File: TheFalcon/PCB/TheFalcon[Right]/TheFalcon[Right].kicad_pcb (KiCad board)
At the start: 4 copper layers, 173.3 x 142.5 mm, 166 parts, among them IC1 IS31FL3729-QFLS4-TR, J1 Conn_01x01, J2 Conn_01x01, J3 Conn_01x01, J4 Conn_01x01, J5 Conn_01x04_Pin, J6 Conn_01x01, J7 Conn_01x01, J8 Conn_01x01, SW1 SW_Push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

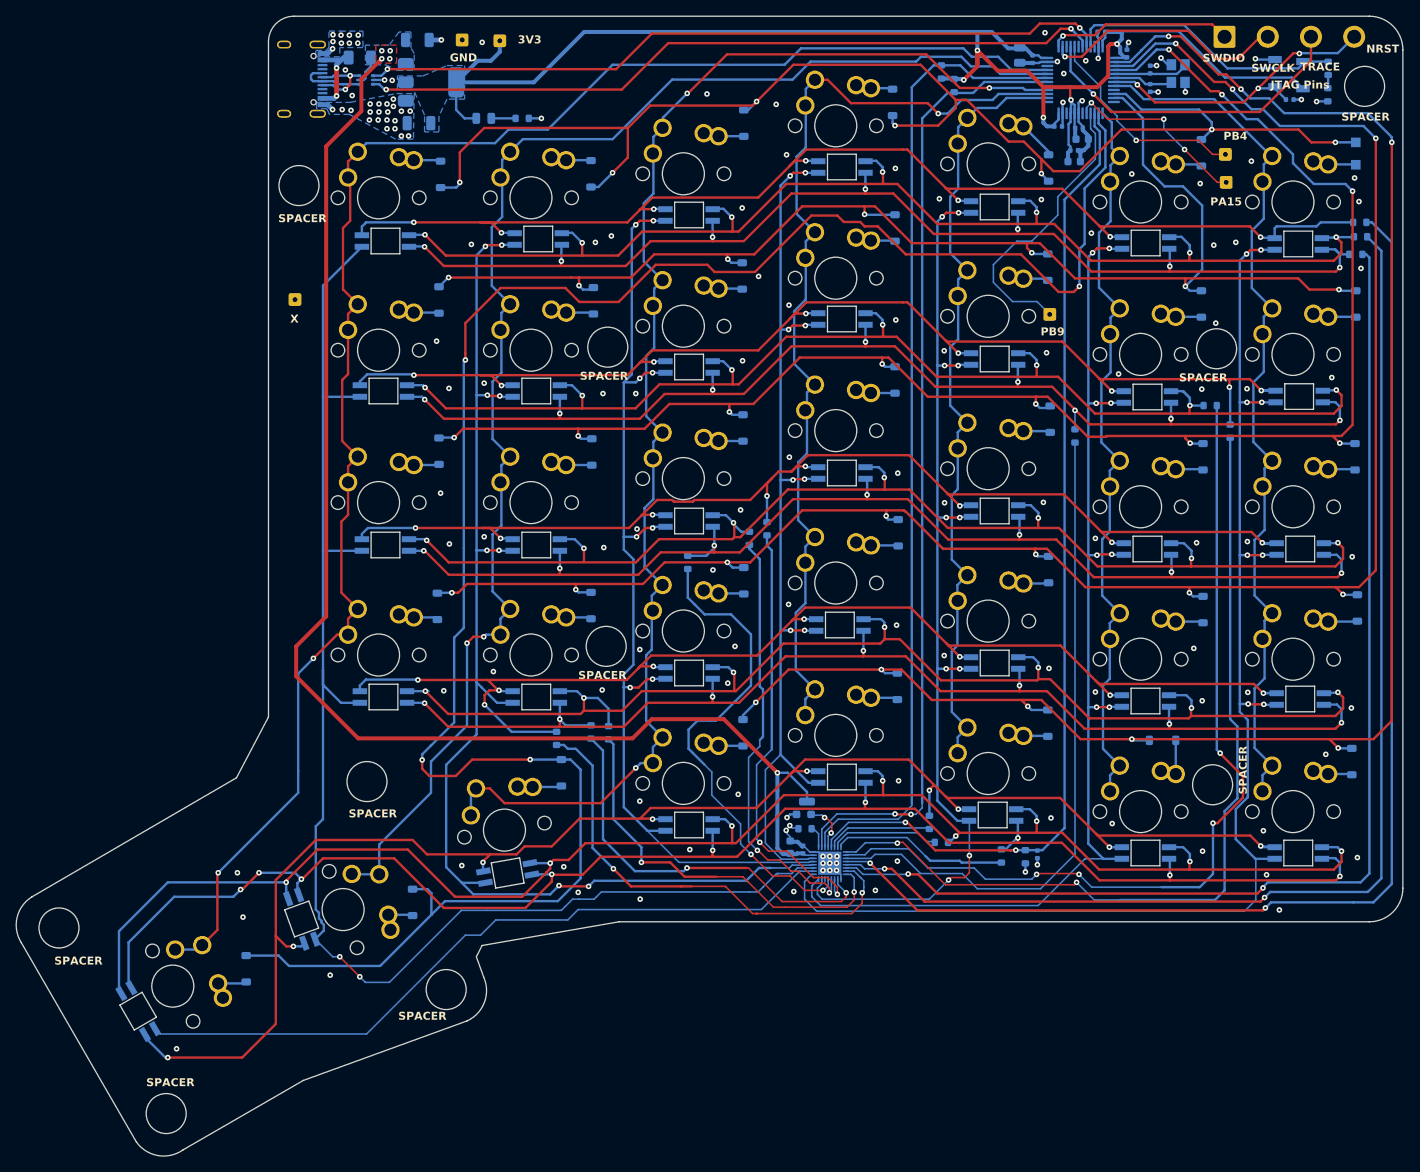
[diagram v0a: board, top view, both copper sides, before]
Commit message: Save
Checked right PCB and hole to track spacing for left. Will do check for left pcb tomorrow
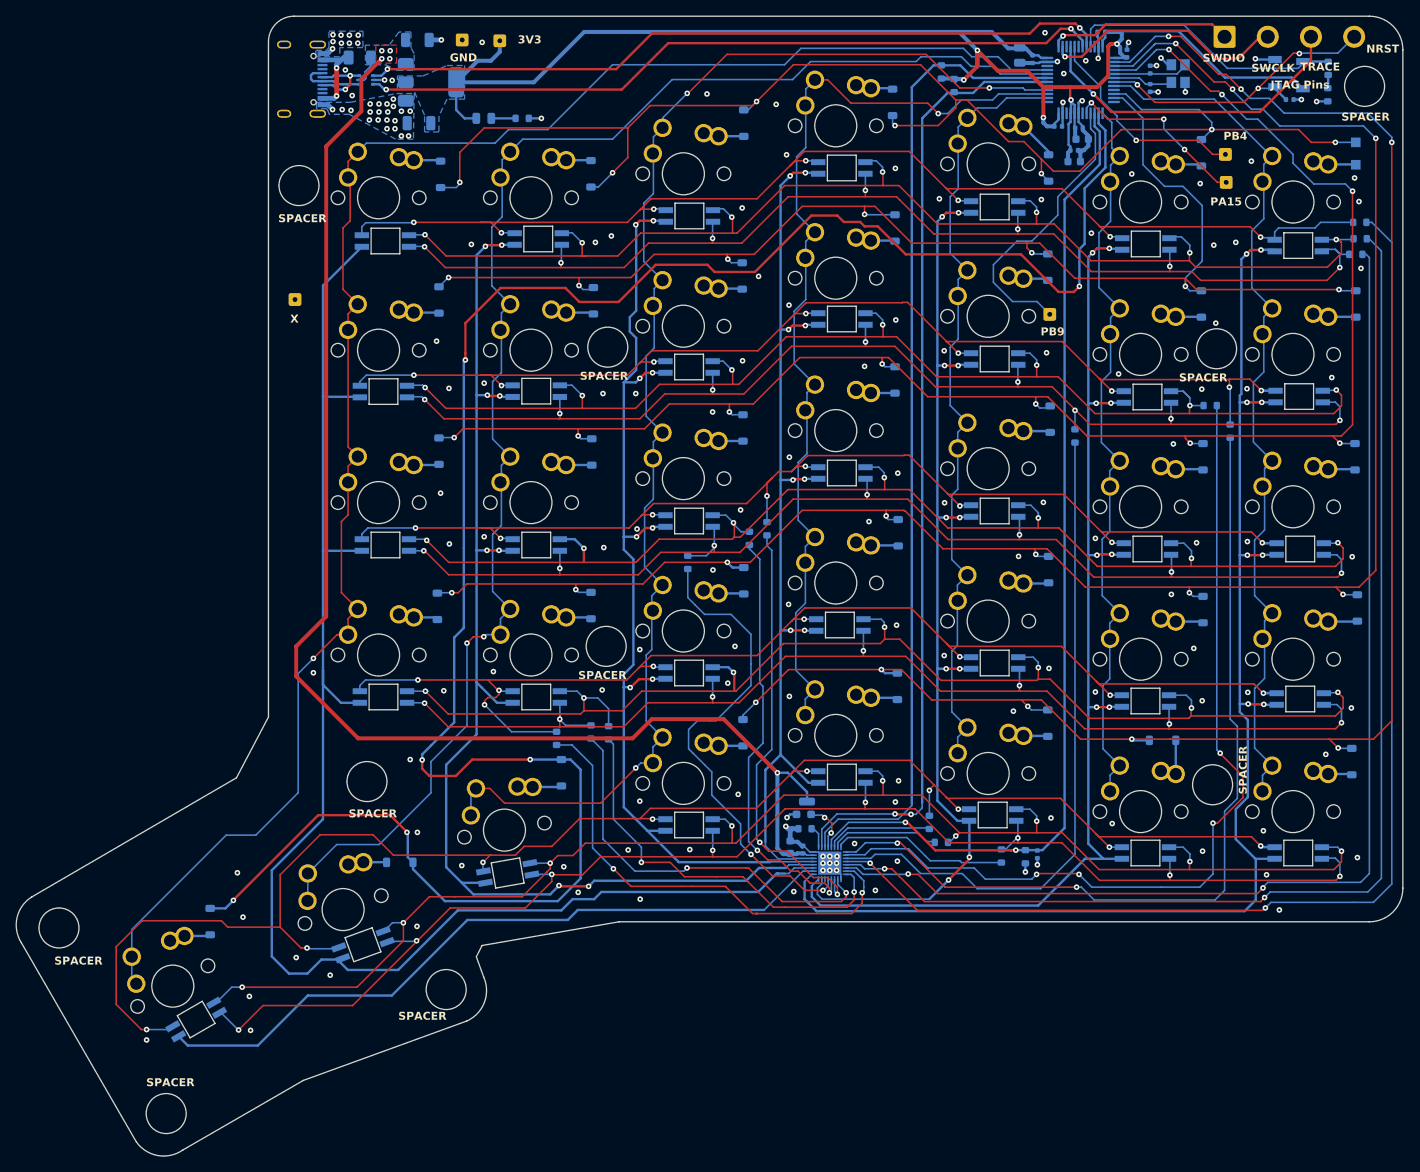
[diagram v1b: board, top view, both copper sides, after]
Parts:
- S35, S36: footprint MX_KS33:MX_KS33-Solderable-1.5U -> MX_KS33:MX_KS33-Solderable-1.5U-Vertical
- moved RGB35 8.31 mm to (88.5, 145.9), turned to 20 degrees
- moved D36 7.42 mm to (69.4, 143.0)
- moved RGB36 7.33 mm to (67.7, 155.2), turned to 30 degrees
- moved D35 5.25 mm to (93.1, 135.6), turned to 180 degrees
- moved R9 0.25 mm to (213.2, 57.6)
- moved RGB1 0.20 mm to (205.4, 58.5)
- moved RGB5 0.13 mm to (129.3, 54.8)
- moved RGB2 0.12 mm to (186.3, 58.3)
- moved RGB4 0.12 mm to (148.3, 48.8)
- moved RGB14 0.07 mm to (91.1, 76.8)
- turned S35 to 20 degrees
- turned S36 to 30 degrees
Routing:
- net /RGB Array/G_RGB_ROW_4: track 207.9 -> 188.6 mm, vias 8 -> 9
- net /RGB Array/R_RGB_ROW_4: track 198.6 -> 182.3 mm, vias 9 -> 8
- net /RGB Array/B_RGB_ROW_4: track 202.6 -> 214.1 mm
- net /RGB Array/SW4: track 177.2 -> 186.1 mm, vias 2 -> 0
- net ThumbRow: track 257.3 -> 264.2 mm, vias 4 -> 6
- net Col1: track 180.9 -> 187.6 mm
- net Col0: track 209.4 -> 216.0 mm, vias 2 -> 1
- net /RGB Array/SW5: track 91.0 -> 88.9 mm
- net +3.3V: track 186.5 -> 188.6 mm
- net /RGB Array/G_RGB_ROW_0: track 155.6 -> 157.3 mm
- net /RGB Array/R_RGB_ROW_0: track 145.2 -> 146.8 mm
- net /RGB Array/SW8: track 124.1 -> 123.1 mm
- net Net-(D36-A): track 4.00 -> 3.32 mm
- net /RGB Array/SW2: track 124.4 -> 124.9 mm
- net GND: track 53.8 -> 54.3 mm, vias 153 -> 170

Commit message: Save
Done checking left and right PCB and case.
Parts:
- added G***: LOGO, LOGO, F.Cu at (75.8, 147.2)
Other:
- board text added: "M.J. Hammon"
- board text added: "The Falcon V1.0 Right Side"

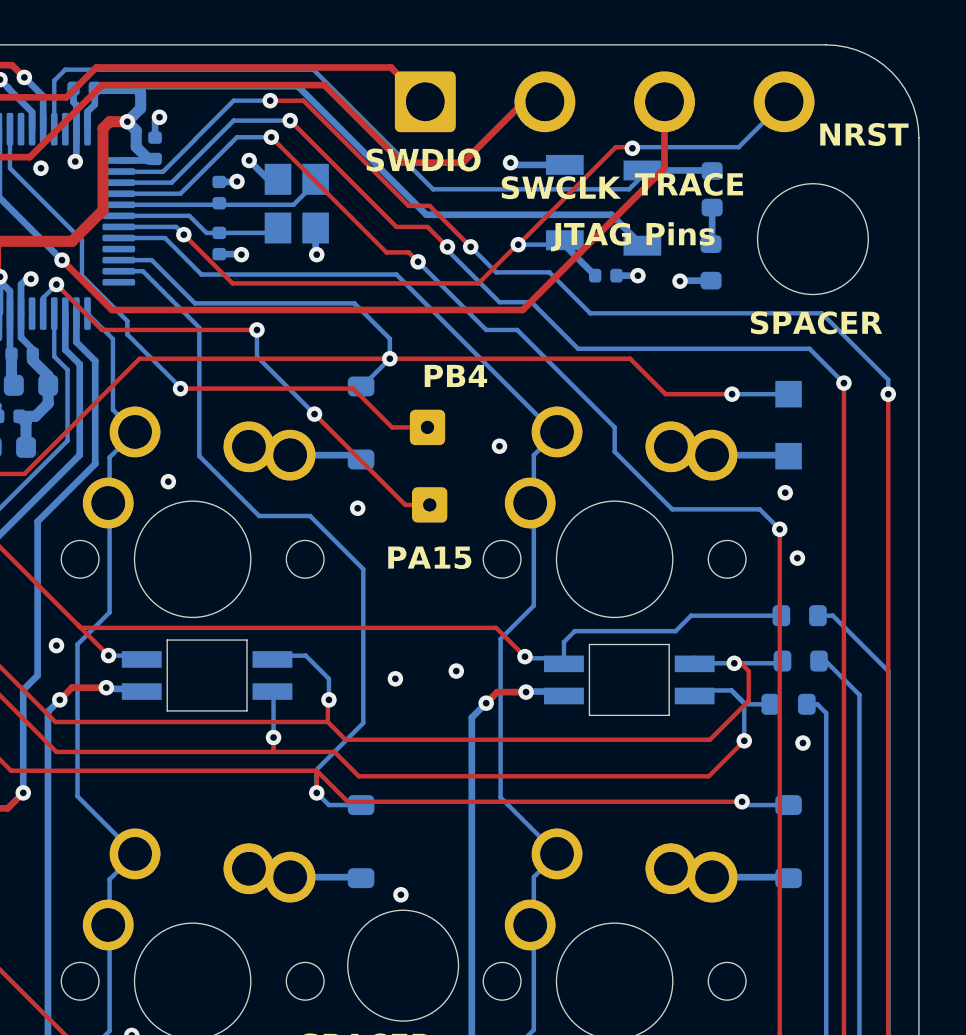
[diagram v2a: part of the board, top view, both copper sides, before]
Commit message: Files ready for production
Going to panelise seperate files to reduce PCBA cost
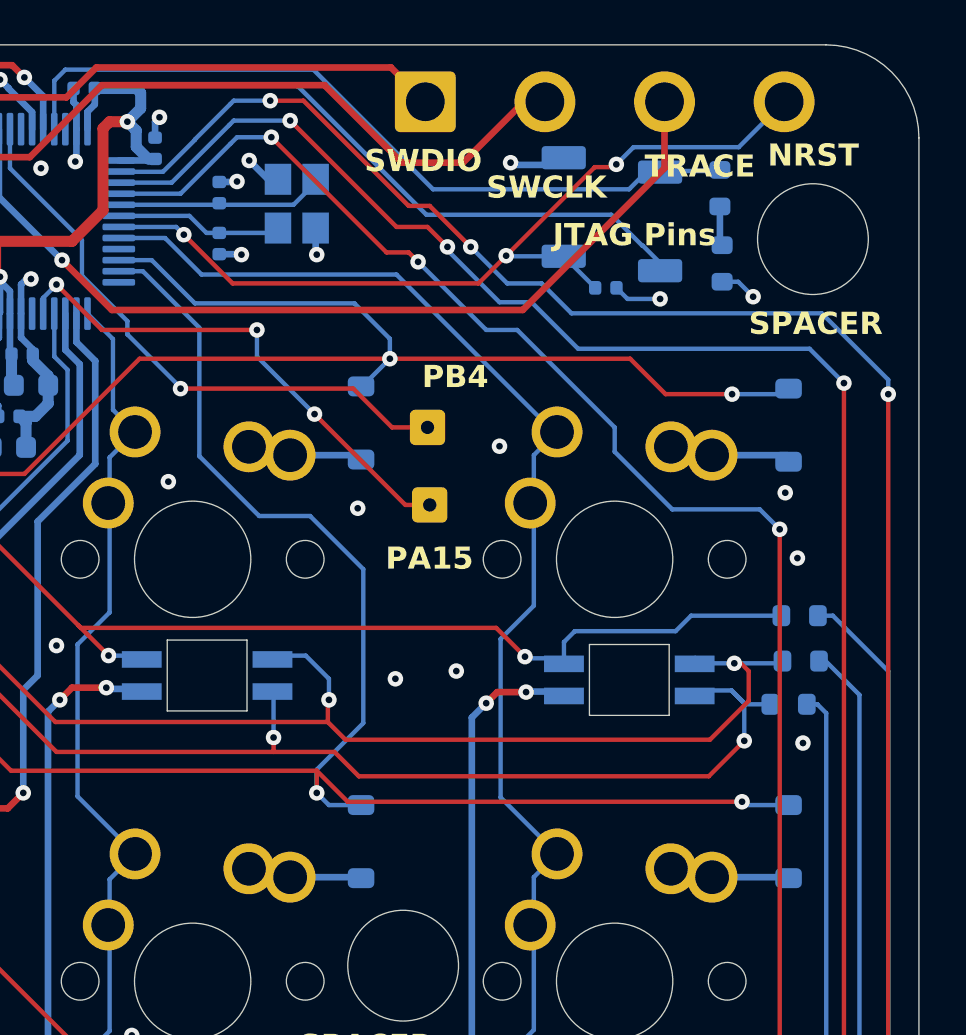
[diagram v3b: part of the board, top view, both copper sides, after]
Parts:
- D1: footprint Diode_SMD:Nexperia_CFP3_SOD-123W -> Diode_SMD:D_SOD-123
- R6, R7: value 5.1k -> 5k1
- SW1, SW2: footprint Button_Switch_SMD:SW_SPST_B3U-1000P -> CustomSPDTButton:SPDT_Switch_KiCad_BasicComponent
- moved SW1 1.00 mm to (206.8, 37.8)
- moved C13 0.55 mm to (204.3, 40.8)
- moved R7 0.50 mm to (209.6, 39.7)
- moved R6 0.35 mm to (209.5, 36.3)
- moved SW2 0.21 mm to (202.4, 37.1)
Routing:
- net GND: track 54.3 -> 55.9 mm
- net +3.3V: track 188.6 -> 190.1 mm
- net BOOT0: track 34.9 -> 33.8 mm
- net (no net): vias 1 -> 0
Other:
- board text added: "BOOT"
